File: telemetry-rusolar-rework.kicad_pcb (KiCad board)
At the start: 4 copper layers, 109.1 x 91.2 mm, 158 parts, among them IC1 TLV62569DBVR, IC3 USBLC6-2P6, IC4 TPS22917DBVR, IC5 TPS22917DBVR, IC6 TPS22917DBVR, J1 USART Debug, J11 USB_B_Micro, J12 I2C, J13 GR2, J14 GR1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

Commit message: Added module LEDs, I2C for Blues Com
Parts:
- added D18: WIFI_HTH, LED_SMD:LED_0805_2012Metric_Pad1.15x1.40mm_HandSolder, F.Cu at (116.6, 110.3)
- added D19: WIFI_ERR, LED_SMD:LED_0805_2012Metric_Pad1.15x1.40mm_HandSolder, F.Cu at (116.6, 112.8)
- added D20: CELLULAR_HTH, LED_SMD:LED_0805_2012Metric_Pad1.15x1.40mm_HandSolder, F.Cu at (116.6, 117.7)
- added D21: CELLULAR_ERR, LED_SMD:LED_0805_2012Metric_Pad1.15x1.40mm_HandSolder, F.Cu at (116.6, 120.3)
- added D22: USR LED1, LED_SMD:LED_0805_2012Metric_Pad1.15x1.40mm_HandSolder, F.Cu at (116.7, 105.4)
- added D23: USR LED2, LED_SMD:LED_0805_2012Metric_Pad1.15x1.40mm_HandSolder, F.Cu at (116.7, 102.9)
- added D4: NOTE_PWR, LED_SMD:LED_0805_2012Metric_Pad1.15x1.40mm_HandSolder, F.Cu at (108.4, 95.7)
- added R27: 1k5, Resistor_SMD:R_0603_1608Metric_Pad0.98x0.95mm_HandSolder, F.Cu at (104.5, 95.7)
- added R43: 470, Resistor_SMD:R_0603_1608Metric_Pad0.98x0.95mm_HandSolder, F.Cu at (120.6, 110.3)
- added R44: 470, Resistor_SMD:R_0603_1608Metric_Pad0.98x0.95mm_HandSolder, F.Cu at (120.6, 112.8)
- added R45: 470, Resistor_SMD:R_0603_1608Metric_Pad0.98x0.95mm_HandSolder, F.Cu at (120.6, 117.7)
- added R46: 470, Resistor_SMD:R_0603_1608Metric_Pad0.98x0.95mm_HandSolder, F.Cu at (120.6, 120.3)
- added R47: 470, Resistor_SMD:R_0603_1608Metric_Pad0.98x0.95mm_HandSolder, F.Cu at (120.6, 105.4)
- added R48: 470, Resistor_SMD:R_0603_1608Metric_Pad0.98x0.95mm_HandSolder, F.Cu at (120.6, 102.9)
- D16: value USER LED 1 -> HEALTH
- D17: value USER LED 2 -> ERR
- turned R12 to 0 degrees
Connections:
- net /PD0 renamed /PD0*
- net /PD1 renamed /PD1*
- net /PD10 renamed /PD10*
- net /PD3 renamed /PD3*
- net /PD4 renamed /PD4*
- net /PD5 renamed /PD5*
- J17 pad 11: /blue-note-card/SDA -> /blue-note-card/SDA_BLUE_PIN
- J17 pad 12: /blue-note-card/SCL -> /blue-note-card/SCL_BLUE_PIN
- J3 pad 40: Net-(J3-Pad40) -> /blue-note-card/SCL_BLUE_PIN
- J3 pad 42: Net-(J3-Pad42) -> /blue-note-card/SDA_BLUE_PIN
- R11 pad 2: Net-(J3-Pad40) -> /blue-note-card/SCL_BLUE_PIN
- R12 pad 1: I2C4_SDA -> /blue-note-card/SDA_BLUE_PIN
- R12 pad 2: Net-(J3-Pad42) -> I2C4_SDA
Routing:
- net /blue-note-card/SCL_BLUE_PIN: track 0.00 -> 98.9 mm, vias 0 -> 2
- net /blue-note-card/SDA_BLUE_PIN: track 0.00 -> 97.8 mm, vias 0 -> 2
- net /PD10*: track 72.9 -> 120.2 mm
- net I2C4_SDA: track 64.6 -> 107.3 mm, vias 1 -> 2
- net /PD0*: track 46.0 -> 86.3 mm
- net I2C4_SCL: track 67.6 -> 106.7 mm, vias 1 -> 2
- net /blue-note-card/SCL: track 35.8 -> 0.00 mm
- net /blue-note-card/SDA: track 33.6 -> 0.00 mm
- net /PD1*: track 47.2 -> 80.2 mm
- net /PD3*: track 45.3 -> 73.4 mm
- net /PD4*: track 50.4 -> 71.1 mm
- net /PD5*: track 51.5 -> 67.7 mm
- net GND: track 205.5 -> 219.9 mm, vias 171 -> 178
- net +3.3V NOTE: track 92.7 -> 96.9 mm
- net Net-(D21-A): track 0.00 -> 2.06 mm
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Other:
- board text added: "*PD10"
- board text added: "*PD12"
- board text added: "*PD13"
- board text added: "CELLULAR"
- board text added: "MODULE STAT"
- board text added: "NOTE_PWR"
- board text added: "PD0*"
- board text added: "PD1*"
- board text added: "PD3*"
- board text added: "PD4*"
- board text added: "PD5*"
- board text added: "QUANG BUI."
- board text added: "RESERVED"
- board text added: "STM32H725VE - BlueNoteCard - ESP32-WROOM-32U"
- board text added: "USR1"
- board text added: "USR2"
- board text added: "WIFI"
- board text added: "v1.3.0"
- board text removed: "PD0"
- board text removed: "PD1"
- board text removed: "PD10"
- board text removed: "PD12"
- board text removed: "PD13"
- board text removed: "PD3"
- board text removed: "PD4"
- board text removed: "PD5"
- board text removed: "QUANG - STM32H725VE - BlueNoteCard - ESP32-WROOM-32U"
- board text removed: "v1.2.0"

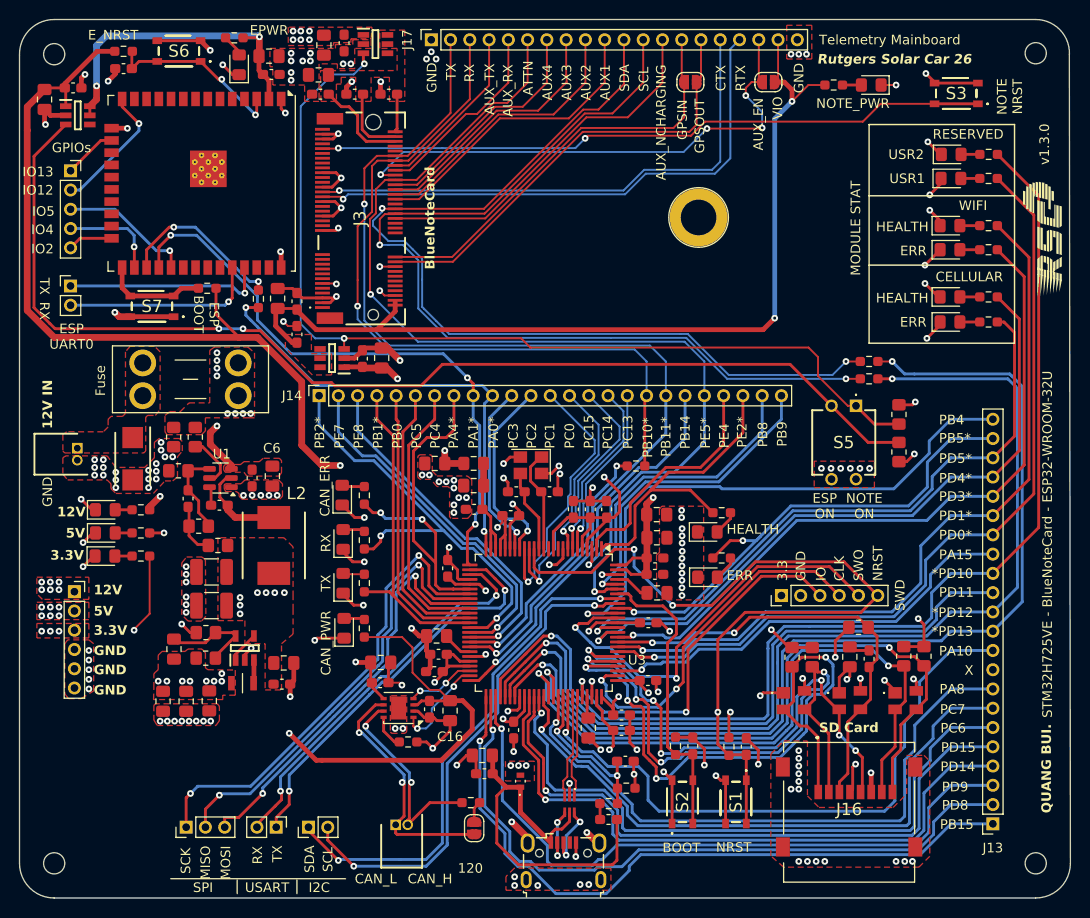
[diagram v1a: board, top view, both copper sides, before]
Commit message: Fixed SD Card layout
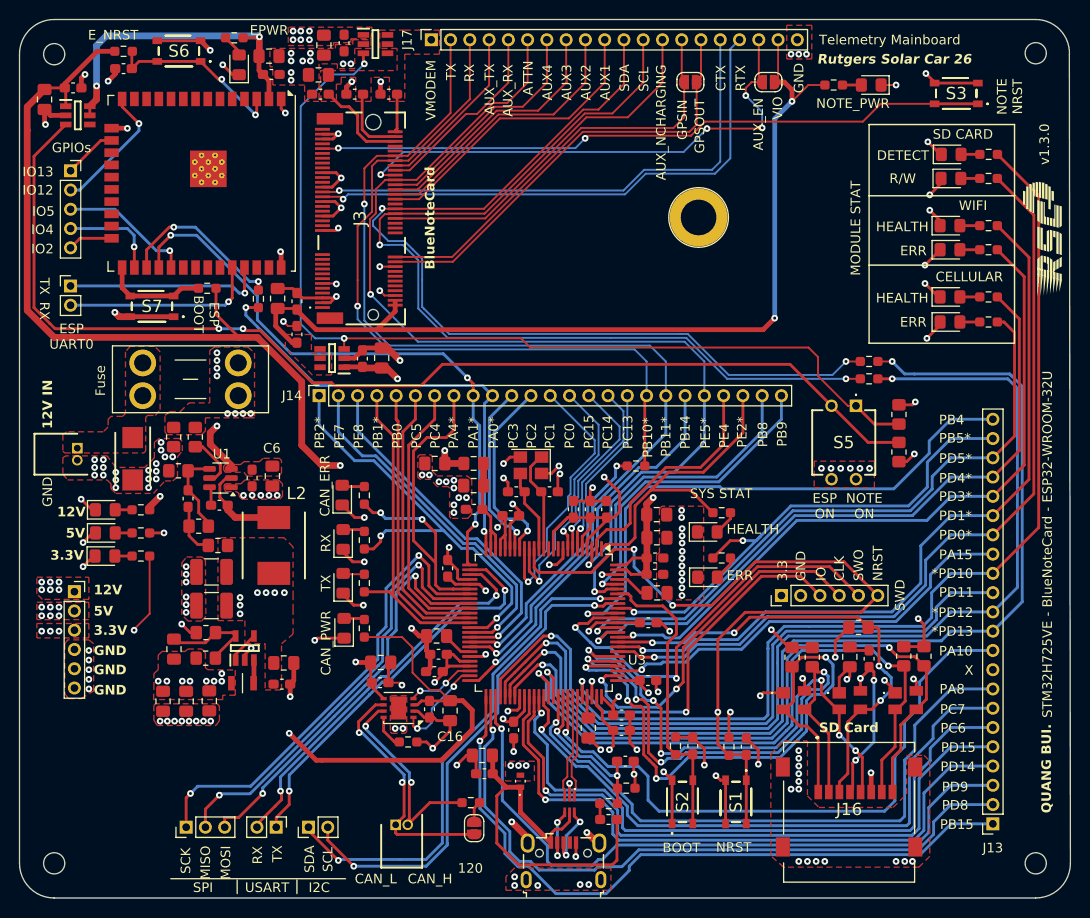
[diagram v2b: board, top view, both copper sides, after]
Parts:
- D22: value USR LED1 -> R/W
- D23: value USR LED2 -> DETECT
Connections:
- C48 pad 1: /SD1_CMD -> +3.3V Buck
- J17 pad 1: GND -> +5V NOTE
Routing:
- net +3.3V Buck: track 218.3 -> 230.9 mm, vias 41 -> 42
- net /SD1_CMD: track 46.8 -> 49.2 mm, vias 2 -> 4
- net GND: vias 178 -> 175
- removed copper zone on In2.Cu, net GND
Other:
- board text added: "DETECT"
- board text added: "R/W"
- board text added: "SD CARD"
- board text added: "SYS STAT"
- board text added: "VMODEM"
- board text removed: "RESERVED"
- board text removed: "USR1"
- board text removed: "USR2"
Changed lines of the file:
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@@
 			)
 		)
-		(property "Value" "USR LED2"
+		(property "Value" "DETECT"
 			(at 0 1.65 0)
 			(layer "F.Fab")
@@
 			)
 		)
-		(property "Value" "USR LED1"
+		(property "Value" "R/W"
 			(at 0 1.65 0)
 			(layer "F.Fab")
@@
 			(layers "F.Cu" "F.Mask" "F.Paste")
 			(roundrect_rratio 0.25)
-			(net 17 "/SD1_CMD")
+			(net 8 "+3.3V Buck")
 			(pintype "passive")
 		)
@@
 			(layers "*.Cu" "*.Mask")
 			(remove_unused_layers no)
-			(net 1 "GND")
+			(net 19 "+5V NOTE")
 			(pinfunction "Pin_1")
 			(pintype "passive")
@@
 	(gr_text "VIO"
 		(at 99.3 99.3 90)
-		(layer "F.SilkS")
+		(layer "F.SilkS" knockout)
 		(effects
 			(font
@@
 		)
 	)
-	(gr_text "USR2"
-		(at 110.2 103.5 0)
+	(gr_text "DETECT"
+		(at 109 103.6 0)
 		(layer "F.SilkS")
 		(effects
@@
 		)
 	)
-	(gr_text "USR1"
+	(gr_text "R/W"
 		(at 110.3 106 0)
 		(layer "F.SilkS")
@@
 		)
 	)
-	(gr_text "PE8"
-		(at 55.8 133.45 90)
-		(layer "F.SilkS")
+	(gr_text "VMODEM"
+		(at 63.3 99.4 90)
+		(layer "F.SilkS" knockout)
 		(effects
 			(font
@@
 		)
 	)
-	(gr_text "BOOT"
-		(at 86.75 175.475 0)
+	(gr_text "PE8"
+		(at 55.8 133.45 90)
 		(layer "F.SilkS")
 		(effects
@@
 		)
 	)
-	(gr_text "GND"
-		(at 63.4 96.5 90)
-		(layer "F.SilkS" knockout)
+	(gr_text "BOOT"
+		(at 86.75 175.475 0)
+		(layer "F.SilkS")
 		(effects
 			(font
@@
 		)
 	)
+	(gr_text "SYS STAT"
+		(at 89.6 138.7 0)
+		(layer "F.SilkS")
+		(effects
+			(font
+				(size 1 1)
+				(thickness 0.15)
+			)
+			(justify left bottom)
+		)
+	)
 	(gr_text "PD14"
 		(at 115.6 167.05 0)
@@
 	(gr_text "GND"
 		(at 101.5 96.55 90)
-		(layer "F.SilkS" knockout)
+		(layer "F.SilkS")
 		(effects
 			(font
@@
 		)
 	)
-	(gr_text "RESERVED"
+	(gr_text "SD CARD"
 		(at 114.8 101.4 0)
 		(layer "F.SilkS")
@@
 	)
 	(via
-		(at 62.75 92.25)
-		(size 0.7)
-		(drill 0.3)
-		(layers "F.Cu" "B.Cu")
-		(free yes)
-		(net 1)
-	)
-	(via
-		(at 62.25 93)
-		(size 0.7)
-		(drill 0.3)
-		(layers "F.Cu" "B.Cu")
-		(free yes)
-		(net 1)
-	)
-	(via
 		(at 54.5 95.351)
 		(size 0.7)
@@
 	)
 	(via
-		(at 63.25 93)
-		(size 0.7)
-		(drill 0.3)
-		(layers "F.Cu" "B.Cu")
-		(free yes)
-		(net 1)
-	)
-	(via
 		(at 27.8 136.2)
 		(size 0.7)
@@
 	)
 	(segment
+		(start 108.2 156.4)
+		(end 107.3 157.3)
+		(width 0.3)
+		(layer "F.Cu")
+		(net 8)
+	)
+	(segment
 		(start 104.689949 153.410051)
 		(end 104.689949 155.103999)
@@
 	)
 	(segment
-		(start 106.22 169.1)
-		(end 106.496 168.824)
-		(width 0.3)
-		(layer "F.Cu")
-		(net 8)
-	)
-	(segment
 		(start 31.9 152.2)
 		(end 31.9 152.3)
@@
 	)
 	(segment
+		(start 106.496 168.824)
+		(end 106.496 166.102318)
+		(width 0.3)
+		(layer "F.Cu")
+		(net 8)
+	)
+	(segment
 		(start 71.8625 139.8625)
 		(end 71.2 139.2)
@@
 	)
 	(segment
+		(start 106.22 169.1)
+		(end 106.496 168.824)
+		(width 0.3)
+		(layer "F.Cu")
+		(net 8)
+	)
+	(segment
 		(start 104.3 136.62)
 		(end 104.3 136.3)
@@
 	)
 	(segment
+		(start 106.496 166.102318)
+		(end 106.801 165.797318)
+		(width 0.3)
+		(layer "F.Cu")
+		(net 8)
+	)
+	(segment
 		(start 66.75 147.525)
 		(end 65.2375 147.525)
@@
 	)
 	(segment
-		(start 106.496 166.504)
-		(end 106.8 166.2)
-		(width 0.3)
-		(layer "F.Cu")
-		(net 8)
-	)
-	(segment
 		(start 93.65 160.95)
 		(end 93.8 160.8)
@@
 	)
 	(segment
+		(start 108.7 156.625)
+		(end 108.2 156.125)
+		(width 0.3)
+		(layer "F.Cu")
+		(net 8)
+	)
+	(segment
+		(start 108.2 156.125)
+		(end 108.2 156.4)
+		(width 0.3)
+		(layer "F.Cu")
+		(net 8)
+	)
+	(segment
 		(start 80.5 161.5625)
 		(end 81.6375 162.7)
@@
 	)
 	(segment
-		(start 106.496 168.824)
-		(end 106.496 166.504)
-		(width 0.3)
-		(layer "F.Cu")
-		(net 8)
-	)
-	(segment
 		(start 66.75 156.025)
 		(end 64.575 156.025)
@@
 	)
 	(segment
+		(start 108.7 157.5)
+		(end 108.7 156.625)
+		(width 0.3)
+		(layer "F.Cu")
+		(net 8)
+	)
+	(segment
 		(start 57.6 125.075)
 		(end 55.7125 125.075)
@@
 	)
 	(via
+		(at 106.801 165.797318)
+		(size 0.7)
+		(drill 0.3)
+		(layers "F.Cu" "B.Cu")
+		(net 8)
+	)
+	(via
 		(at 68.4 148.2)
 		(size 0.7)
@@
 	)
 	(via
+		(at 108.7 157.5)
+		(size 0.7)
+		(drill 0.3)
+		(layers "F.Cu" "B.Cu")
+		(net 8)
+	)
+	(via
 		(at 63.1 157.7)
 		(size 0.7)
@@
 		(net 8)
 	)
-	(via
-		(at 106.8 166.2)
-		(size 0.7)
-		(drill 0.3)
-		(layers "F.Cu" "B.Cu")
+	(segment
+		(start 108.7 163.898318)
+		(end 108.7 157.5)
+		(width 0.3)
+		(layer "B.Cu")
+		(net 8)
+	)
+	(segment
+		(start 106.801 165.797318)
+		(end 108.7 163.898318)
+		(width 0.3)
+		(layer "B.Cu")
 		(net 8)
 	)
@@
 	)
 	(segment
-		(start 108.2 156.125)
-		(end 109.026 155.299)
+		(start 109.225 152.225)
+		(end 109 152)
 		(width 0.3)
 		(layer "F.Cu")
@@
 	)
 	(segment
-		(start 109.026 152.926)
-		(end 108.1 152)
-		(width 0.3)
-		(layer "F.Cu")
-		(net 17)
-	)
-	(segment
-		(start 108.351 159.469)
-		(end 108.351 156.276)
+		(start 108.48 160.52)
+		(end 109.4 159.6)
 		(width 0.3)
 		(layer "F.Cu")
@@
 	)
 	(segment
-		(start 109.026 155.299)
-		(end 109.026 152.926)
-		(width 0.3)
-		(layer "F.Cu")
-		(net 17)
-	)
-	(segment
-		(start 108.351 156.276)
-		(end 108.2 156.125)
+		(start 107.3 160.52)
+		(end 108.48 160.52)
 		(width 0.3)
 		(layer "F.Cu")
@@
 	)
 	(segment
-		(start 107.3 160.52)
-		(end 108.351 159.469)
+		(start 109 152)
+		(end 108.1 152)
 		(width 0.3)
 		(layer "F.Cu")
@@
 	)
 	(segment
+		(start 109.225 156.014949)
+		(end 109.225 152.225)
+		(width 0.3)
+		(layer "F.Cu")
+		(net 17)
+	)
+	(segment
 		(start 105.995 161.825)
 		(end 105.995 167.175)
@@
 	)
 	(via
+		(at 109.225 156.014949)
+		(size 0.7)
+		(drill 0.3)
+		(layers "F.Cu" "B.Cu")
+		(net 17)
+	)
+	(via
+		(at 109.4 159.6)
+		(size 0.7)
+		(drill 0.3)
+		(layers "F.Cu" "B.Cu")
+		(net 17)
+	)
+	(via
 		(at 94.2 152.56974)
 		(size 0.7)
@@
 	)
 	(segment
+		(start 109.4 159.6)
+		(end 110.501 158.499)
+		(width 0.3)
+		(layer "B.Cu")
+		(net 17)
+	)
+	(segment
+		(start 109.992364 156.701)
+		(end 109.911051 156.701)
+		(width 0.3)
+		(layer "B.Cu")
+		(net 17)
+	)
+	(segment
+		(start 110.501 158.499)
+		(end 110.501 157.209636)
+		(width 0.3)
+		(layer "B.Cu")
+		(net 17)
+	)
+	(segment
+		(start 110.501 157.209636)
+		(end 109.992364 156.701)
+		(width 0.3)
+		(layer "B.Cu")
+		(net 17)
+	)
+	(segment
 		(start 85.7 153.6)
 		(end 89.08296 153.6)
@@
 	)
 	(segment
+		(start 109.911051 156.701)
+		(end 109.225 156.014949)
+		(width 0.3)
+		(layer "B.Cu")
+		(net 17)
+	)
+	(segment
 		(start 108.2 154.4)
 		(end 106.575 154.4)
@@
 		(polygon
 			(pts
-				(xy 57.4 91.9) (xy 57.4 90) (xy 60 90) (xy 60 95.3) (xy 60 97.4) (xy 58.4 97.4) (xy 58.4 94.9) (xy 56.5 94.9)
-				(xy 56.5 97.4) (xy 54.9 97.4) (xy 54.9 94.9) (xy 53.4 94.9) (xy 53.4 95.6) (xy 52.9 95.6) (xy 52.9 97.4)
-				(xy 51.3 97.4) (xy 51.245947 94.2) (xy 59.2 94.2) (xy 59.2 91.9)
+				(xy 57.4 91.9) (xy 57.4 90) (xy 60 90) (xy 63.6 90) (xy 63.6 92.5) (xy 60 92.5) (xy 60 97.4) (xy 58.4 97.4)
+				(xy 58.4 94.9) (xy 56.5 94.9) (xy 56.5 97.4) (xy 54.9 97.4) (xy 54.9 94.9) (xy 53.4 94.9) (xy 53.4 95.6)
+				(xy 52.9 95.6) (xy 52.9 97.4) (xy 51.3 97.4) (xy 51.245947 94.2) (xy 59.2 94.2) (xy 59.2 91.9)
 			)
 		)
@@
 			)
 		)
-	)
-	(zone
-		(net 1)
-		(net_name "GND")
-		(layer "In2.Cu")
-		(hatch edge 0.5)
-		(priority 5)
-		(connect_pads yes
-			(clearance 0.3)
-		)
-		(min_thickness 0.25)
-		(filled_areas_thickness no)
-		(fill yes
-			(thermal_gap 0.5)
-			(thermal_bridge_width 0.5)
-		)
-		(polygon
-			(pts
-				(xy 61.5 93.1875) (xy 61.8125 93.5) (xy 63.578125 93.5) (xy 63.75 93.328125) (xy 63.75 89.5) (xy 61.5 89.5)
-			)
-		)
